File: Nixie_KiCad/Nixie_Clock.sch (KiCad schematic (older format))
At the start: 34 parts, among them U1 K155ID1, U10 K155ID1, U11 IN-14, U12 K155ID1, U13 IN-14, U14 DS3231, U2 IN-14, U3 K155ID1, U4 IN-14, U5 K155ID1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

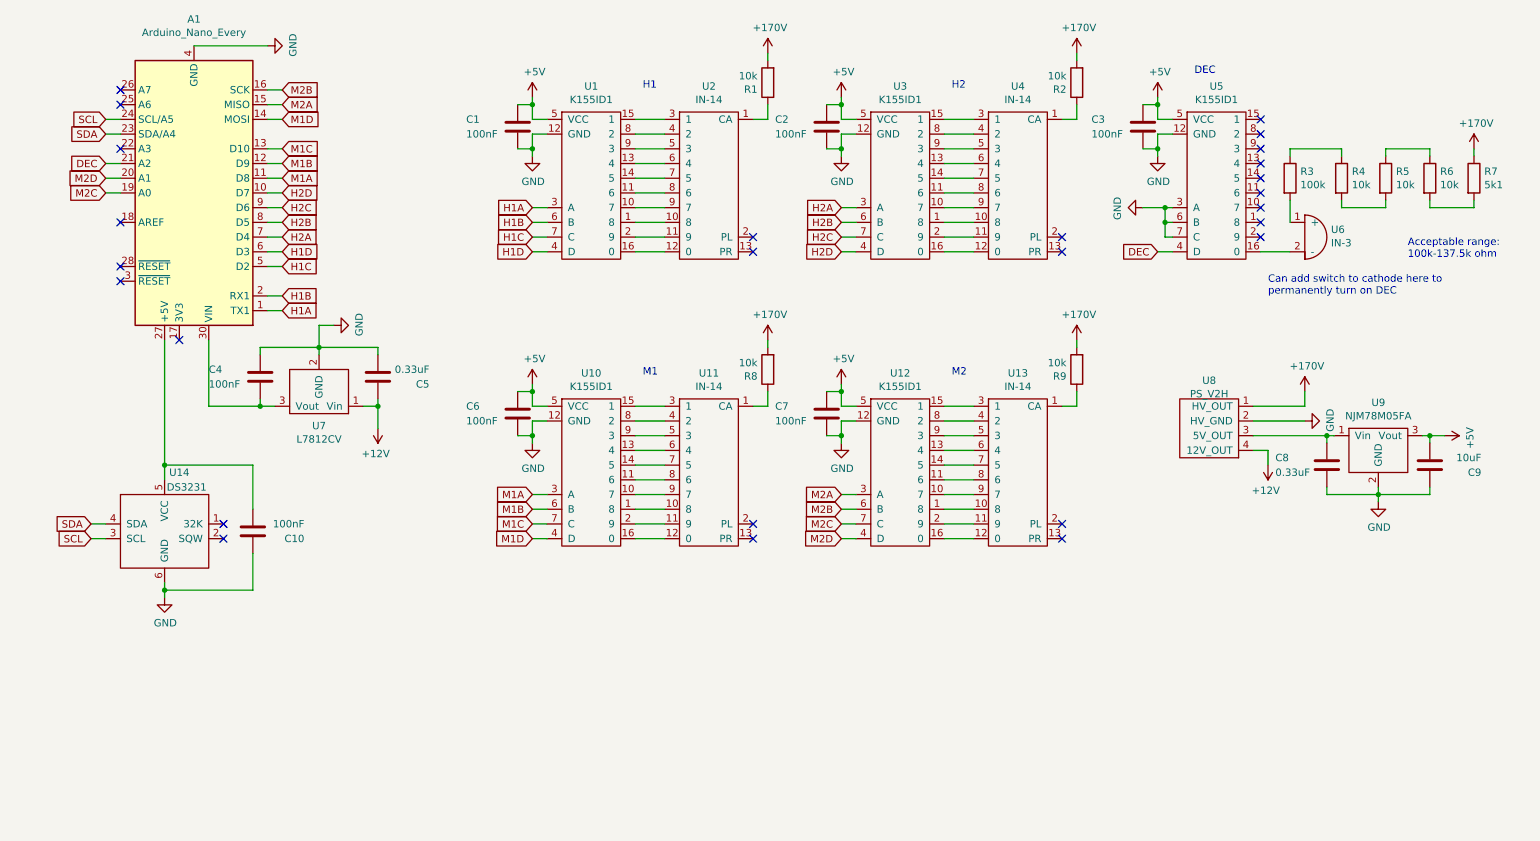
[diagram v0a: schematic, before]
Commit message: updated schematic to 2.0
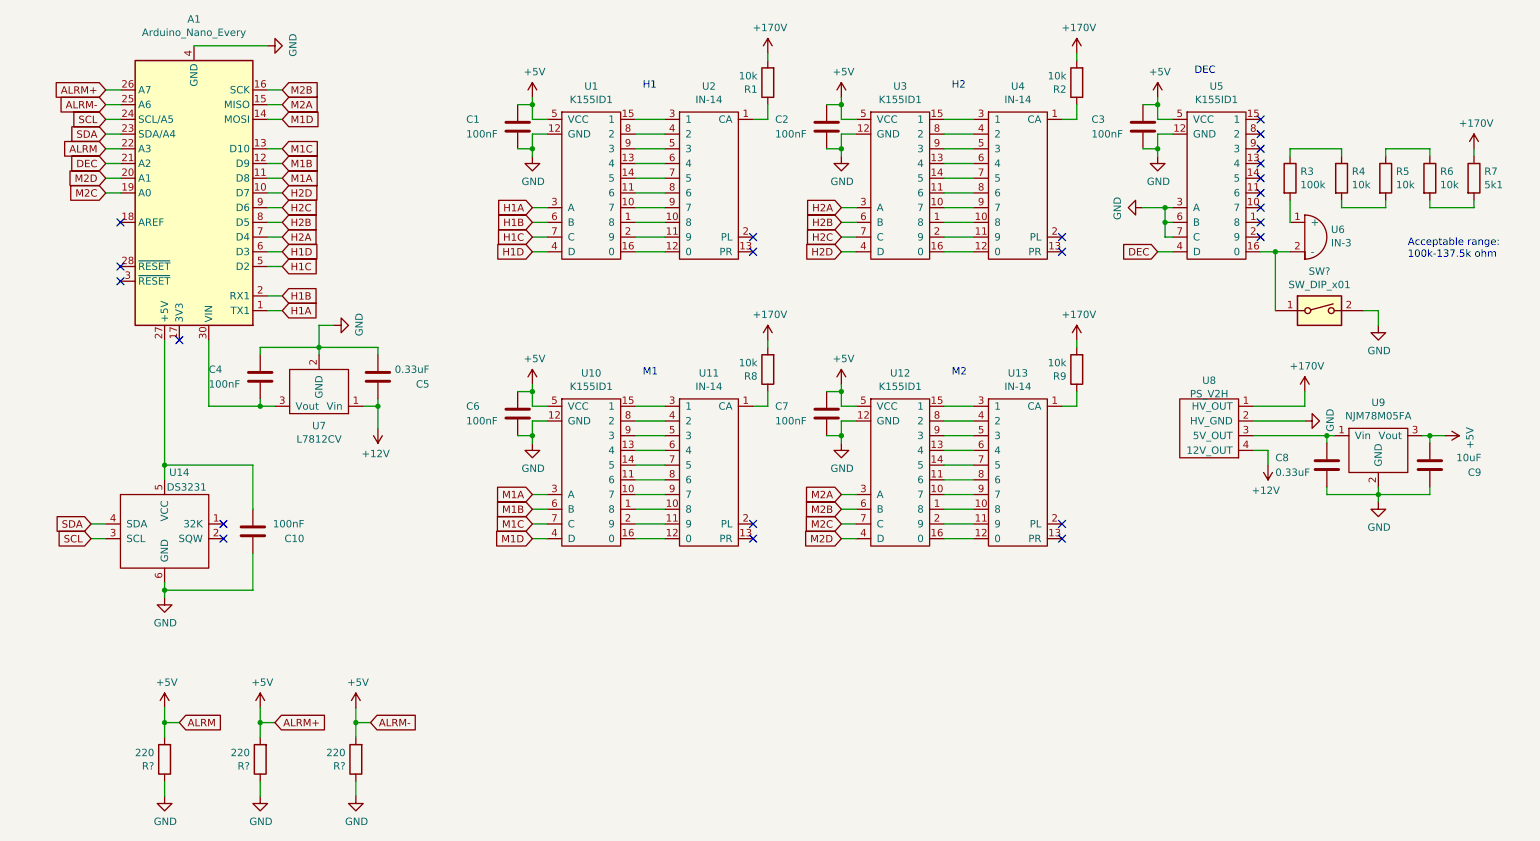
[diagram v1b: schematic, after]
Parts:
- added R? (x3): 220, Resistor_THT:R_Axial_DIN0207_L6.3mm_D2.5mm_P7.62mm_Horizontal, symbol Device:R
- added SW?: SW_DIP_x01, symbol Switch:SW_DIP_x01
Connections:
- net +5V: now also A1.22 (A3), A1.25 (A6), A1.26 (A7), R?.2, R?.2, R?.2
- net GND: now also R?.1, R?.1, R?.1, SW?.2
- net at U5.16 (0), U6.2 (-): now also SW?.1
- no-connect marks 26 -> 23
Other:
- note removed: "Can add switch to cathode here to\npermanently turn on DEC"
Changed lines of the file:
@@
 Title "Nixie Clock"
 Date "2022-01-07"
-Rev "1.1.1"
+Rev "2.0"
 Comp "Michael Zheng"
 Comment1 ""
@@
 $EndComp
 Wire Wire Line
-	9150 3450 8950 3450
+	9150 3450 9050 3450
 $Comp
 L Nixie_Lib:+170V #PWR017
@@
 Wire Wire Line
 	10400 2750 10400 2800
-Text Notes 9000 3750 0    50   ~ 0
-Can add switch to cathode here to\npermanently turn on DEC
 Wire Wire Line
 	2300 2450 2200 2450
 Wire Wire Line
 	2200 2350 2300 2350
-NoConn ~ 1200 2350
-NoConn ~ 1200 2450
-NoConn ~ 1200 2750
 NoConn ~ 1200 3250
 NoConn ~ 1200 3550
 NoConn ~ 1200 3650
 NoConn ~ 1600 4050
-$Comp
-L Nixie_Lib:Arduino_Nano_Every A1
-U 1 1 61EA91F0
-P 1700 3050
-F 0 "A1" H 1700 1869 50  0000 C CNN
-F 1 "Arduino_Nano_Every" H 1700 1960 50  0000 C CNN
-F 2 "Module:Arduino_Nano" H 1700 3050 50  0001 C CIN
-F 3 "https://content.arduino.cc/assets/NANOEveryV3.0_sch.pdf" H 1700 3050 50  0001 C CNN
-	1    1700 3050
-	-1   0    0    1
-$EndComp
 $Comp
 L power:GND #PWR024
@@
 Wire Wire Line
 	1100 2550 1200 2550
+$Comp
+L Switch:SW_DIP_x01 SW?
+U 1 1 61DB88E1
+P 9350 3850
+F 0 "SW?" H 9350 4117 50  0000 C CNN
+F 1 "SW_DIP_x01" H 9350 4026 50  0000 C CNN
+F 2 "" H 9350 3850 50  0001 C CNN
+F 3 "~" H 9350 3850 50  0001 C CNN
+	1    9350 3850
+	1    0    0    -1
+$EndComp
+Connection ~ 9050 3450
+Wire Wire Line
+	9050 3450 8950 3450
+$Comp
+L power:GND #PWR?
+U 1 1 61DC508D
+P 9750 3950
+F 0 "#PWR?" H 9750 3700 50  0001 C CNN
+F 1 "GND" H 9755 3777 50  0000 C CNN
+F 2 "" H 9750 3950 50  0001 C CNN
+F 3 "" H 9750 3950 50  0001 C CNN
+	1    9750 3950
+	1    0    0    -1
+$EndComp
+Wire Wire Line
+	9050 3450 9050 3850
+Wire Wire Line
+	9650 3850 9750 3850
+Wire Wire Line
+	9750 3850 9750 3950
+Text GLabel 1100 2750 0    50   Input ~ 0
+ALRM
+Text GLabel 1100 2350 0    50   Input ~ 0
+ALRM+
+Text GLabel 1100 2450 0    50   Input ~ 0
+ALRM-
+Wire Wire Line
+	1100 2350 1200 2350
+$Comp
+L Nixie_Lib:Arduino_Nano_Every A1
+U 1 1 61EA91F0
+P 1700 3050
+F 0 "A1" H 1700 1869 50  0000 C CNN
+F 1 "Arduino_Nano_Every" H 1700 1960 50  0000 C CNN
+F 2 "Module:Arduino_Nano" H 1700 3050 50  0001 C CIN
+F 3 "https://content.arduino.cc/assets/NANOEveryV3.0_sch.pdf" H 1700 3050 50  0001 C CNN
+	1    1700 3050
+	-1   0    0    1
+$EndComp
+Wire Wire Line
+	1100 2450 1200 2450
+Wire Wire Line
+	1100 2750 1200 2750
+$Comp
+L Device:R R?
+U 1 1 61E7D12A
+P 1500 6900
+F 0 "R?" H 1570 6946 50  0000 L CNN
+F 1 "220" H 1570 6855 50  0000 L CNN
+F 2 "Resistor_THT:R_Axial_DIN0207_L6.3mm_D2.5mm_P7.62mm_Horizontal" V 1430 6900 50  0001 C CNN
+F 3 "~" H 1500 6900 50  0001 C CNN
+	1    1500 6900
+	-1   0    0    1
+$EndComp
+$Comp
+L power:GND #PWR?
+U 1 1 61E7D6BF
+P 1500 7150
+F 0 "#PWR?" H 1500 6900 50  0001 C CNN
+F 1 "GND" H 1505 6977 50  0000 C CNN
+F 2 "" H 1500 7150 50  0001 C CNN
+F 3 "" H 1500 7150 50  0001 C CNN
+	1    1500 7150
+	1    0    0    -1
+$EndComp
+$Comp
+L power:+5V #PWR?
+U 1 1 61E8ADEA
+P 1500 6550
+F 0 "#PWR?" H 1500 6400 50  0001 C CNN
+F 1 "+5V" H 1515 6723 50  0000 C CNN
+F 2 "" H 1500 6550 50  0001 C CNN
+F 3 "" H 1500 6550 50  0001 C CNN
+	1    1500 6550
+	1    0    0    -1
+$EndComp
+Wire Wire Line
+	1500 7150 1500 7050
+Wire Wire Line
+	1500 6550 1500 6650
+Text GLabel 1600 6650 2    50   Input ~ 0
+ALRM
+Wire Wire Line
+	1500 6650 1600 6650
+Connection ~ 1500 6650
+Wire Wire Line
+	1500 6650 1500 6750
+$Comp
+L Device:R R?
+U 1 1 61EC38AF
+P 2150 6900
+F 0 "R?" H 2220 6946 50  0000 L CNN
+F 1 "220" H 2220 6855 50  0000 L CNN
+F 2 "Resistor_THT:R_Axial_DIN0207_L6.3mm_D2.5mm_P7.62mm_Horizontal" V 2080 6900 50  0001 C CNN
+F 3 "~" H 2150 6900 50  0001 C CNN
+	1    2150 6900
+	-1   0    0    1
+$EndComp
+$Comp
+L power:+5V #PWR?
+U 1 1 61EC3F05
+P 2150 6550
+F 0 "#PWR?" H 2150 6400 50  0001 C CNN
+F 1 "+5V" H 2165 6723 50  0000 C CNN
+F 2 "" H 2150 6550 50  0001 C CNN
+F 3 "" H 2150 6550 50  0001 C CNN
+	1    2150 6550
+	1    0    0    -1
+$EndComp
+$Comp
+L power:GND #PWR?
+U 1 1 61EC4290
+P 2150 7150
+F 0 "#PWR?" H 2150 6900 50  0001 C CNN
+F 1 "GND" H 2155 6977 50  0000 C CNN
+F 2 "" H 2150 7150 50  0001 C CNN
+F 3 "" H 2150 7150 50  0001 C CNN
+	1    2150 7150
+	1    0    0    -1
+$EndComp
+Wire Wire Line
+	2150 6550 2150 6650
+Wire Wire Line
+	2150 7050 2150 7150
+Wire Wire Line
+	2150 6650 2250 6650
+Connection ~ 2150 6650
+Wire Wire Line
+	2150 6650 2150 6750
+Text GLabel 2250 6650 2    50   Input ~ 0
+ALRM+
+$Comp
+L Device:R R?
+U 1 1 61EFBDFE
+P 2800 6900
+F 0 "R?" H 2870 6946 50  0000 L CNN
+F 1 "220" H 2870 6855 50  0000 L CNN
+F 2 "Resistor_THT:R_Axial_DIN0207_L6.3mm_D2.5mm_P7.62mm_Horizontal" V 2730 6900 50  0001 C CNN
+F 3 "~" H 2800 6900 50  0001 C CNN
+	1    2800 6900
+	-1   0    0    1
+$EndComp
+$Comp
+L power:+5V #PWR?
+U 1 1 61EFCF7D
+P 2800 6550
+F 0 "#PWR?" H 2800 6400 50  0001 C CNN
+F 1 "+5V" H 2815 6723 50  0000 C CNN
+F 2 "" H 2800 6550 50  0001 C CNN
+F 3 "" H 2800 6550 50  0001 C CNN
+	1    2800 6550
+	1    0    0    -1
+$EndComp
+$Comp
+L power:GND #PWR?
+U 1 1 61EFD250
+P 2800 7150
+F 0 "#PWR?" H 2800 6900 50  0001 C CNN
+F 1 "GND" H 2805 6977 50  0000 C CNN
+F 2 "" H 2800 7150 50  0001 C CNN
+F 3 "" H 2800 7150 50  0001 C CNN
+	1    2800 7150
+	1    0    0    -1
+$EndComp
+Wire Wire Line
+	2800 7050 2800 7150
+Wire Wire Line
+	2800 6750 2800 6650
+Wire Wire Line
+	2800 6650 2900 6650
+Connection ~ 2800 6650
+Wire Wire Line
+	2800 6650 2800 6550
+Text GLabel 2900 6650 2    50   Input ~ 0
+ALRM-
 $EndSCHEMATC

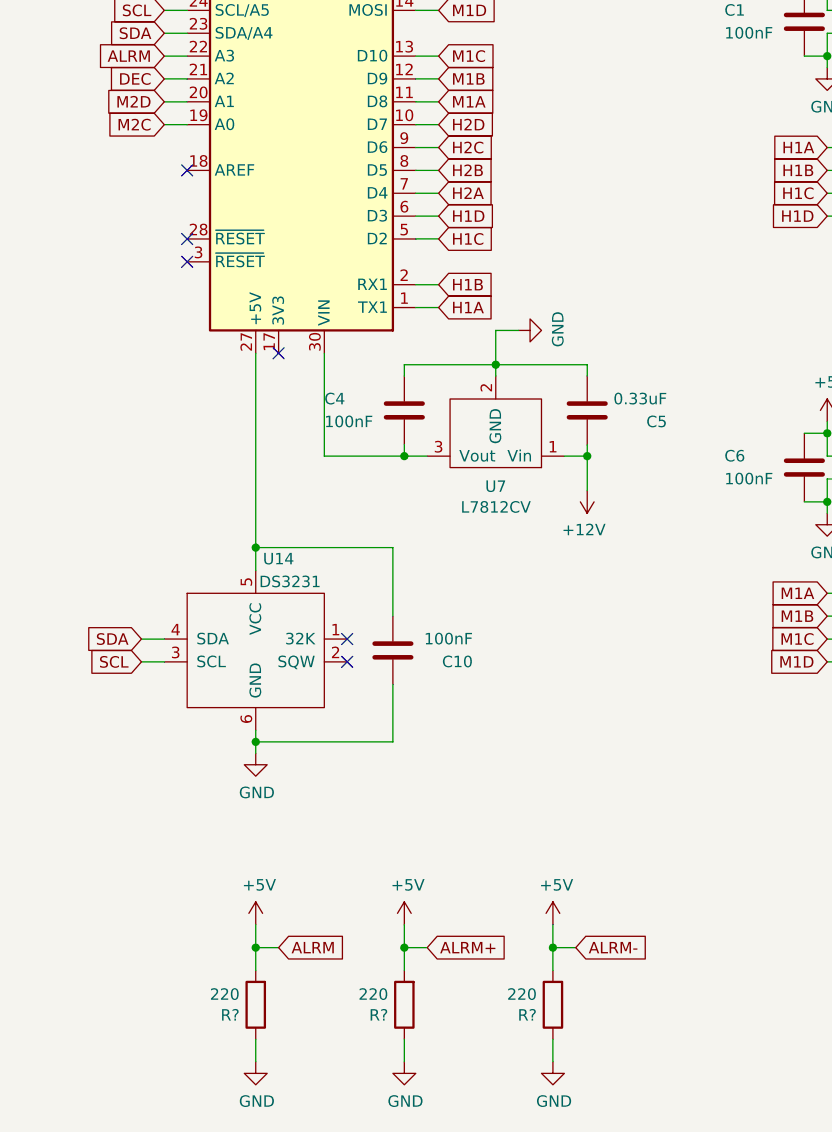
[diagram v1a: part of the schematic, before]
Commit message: updated to internal pull up resistors
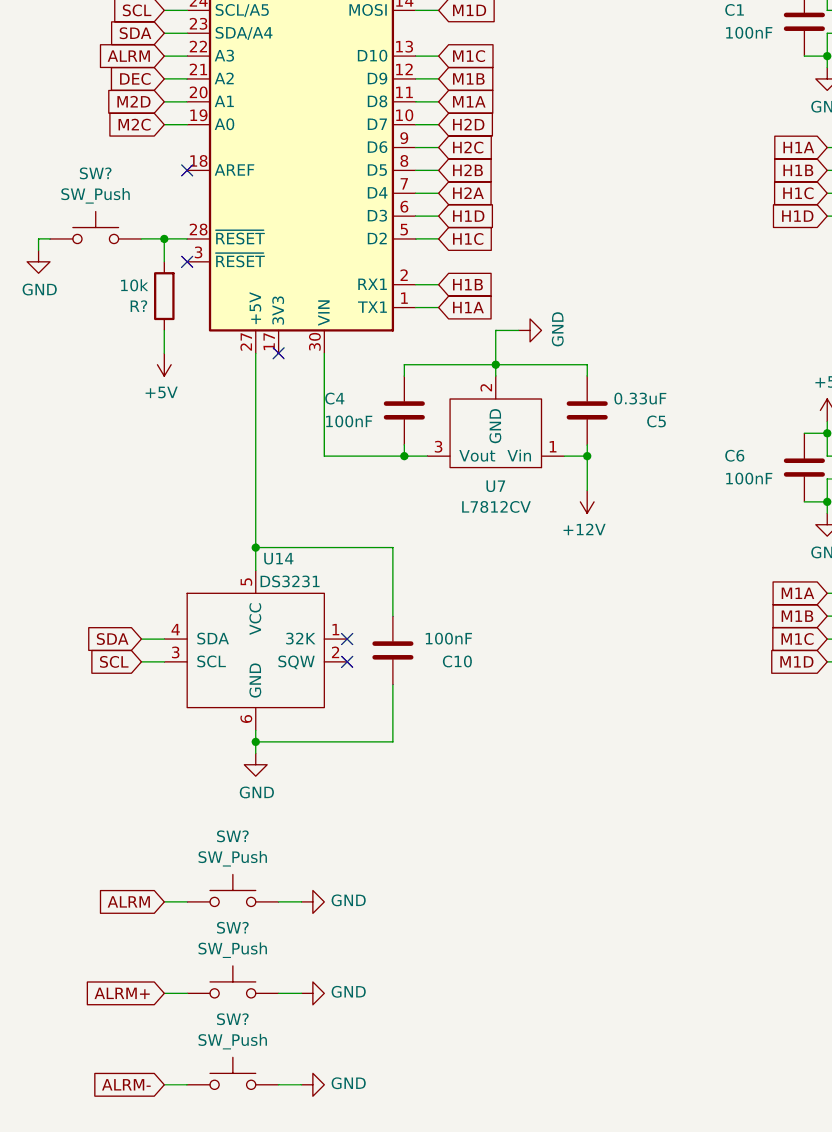
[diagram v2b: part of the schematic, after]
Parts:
- removed R? (x3): 220, Resistor_THT:R_Axial_DIN0207_L6.3mm_D2.5mm_P7.62mm_Horizontal, symbol Device:R
- added R?: 10k, Resistor_THT:R_Axial_DIN0207_L6.3mm_D2.5mm_P7.62mm_Horizontal, symbol Device:R
- added SW? (x4): SW_Push, symbol Switch:SW_Push
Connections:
- net +5V: now also R?.1; no longer A1.22 (A3), A1.25 (A6), A1.26 (A7)
- net GND: now also SW?.1, SW?.2, SW?.2, SW?.2
- net at A1.28 (~RESET): now also R?.2, SW?.2
- new net ALRM: A1.22 (A3), SW?.1
- new net ALRM+: A1.26 (A7), SW?.1
- new net ALRM-: A1.25 (A6), SW?.1
- no-connect marks 23 -> 22
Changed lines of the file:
@@
 	2200 2350 2300 2350
 NoConn ~ 1200 3250
-NoConn ~ 1200 3550
 NoConn ~ 1200 3650
 NoConn ~ 1600 4050
@@
 Wire Wire Line
 	1100 2750 1200 2750
+Text GLabel 1100 6450 0    50   Input ~ 0
+ALRM
+Text GLabel 1100 6850 0    50   Input ~ 0
+ALRM+
+Text GLabel 1100 7250 0    50   Input ~ 0
+ALRM-
+$Comp
+L Switch:SW_Push SW?
+U 1 1 61E3B7EB
+P 1400 6450
+F 0 "SW?" H 1400 6735 50  0000 C CNN
+F 1 "SW_Push" H 1400 6644 50  0000 C CNN
+F 2 "" H 1400 6650 50  0001 C CNN
+F 3 "~" H 1400 6650 50  0001 C CNN
+	1    1400 6450
+	1    0    0    -1
+$EndComp
+$Comp
+L power:GND #PWR?
+U 1 1 61E64086
+P 1700 6450
+F 0 "#PWR?" H 1700 6200 50  0001 C CNN
+F 1 "GND" V 1705 6322 50  0000 R CNN
+F 2 "" H 1700 6450 50  0001 C CNN
+F 3 "" H 1700 6450 50  0001 C CNN
+	1    1700 6450
+	0    -1   -1   0
+$EndComp
+$Comp
+L Switch:SW_Push SW?
+U 1 1 61E66E38
+P 1400 6850
+F 0 "SW?" H 1400 7135 50  0000 C CNN
+F 1 "SW_Push" H 1400 7044 50  0000 C CNN
+F 2 "" H 1400 7050 50  0001 C CNN
+F 3 "~" H 1400 7050 50  0001 C CNN
+	1    1400 6850
+	1    0    0    -1
+$EndComp
+$Comp
+L Switch:SW_Push SW?
+U 1 1 61E67592
+P 1400 7250
+F 0 "SW?" H 1400 7535 50  0000 C CNN
+F 1 "SW_Push" H 1400 7444 50  0000 C CNN
+F 2 "" H 1400 7450 50  0001 C CNN
+F 3 "~" H 1400 7450 50  0001 C CNN
+	1    1400 7250
+	1    0    0    -1
+$EndComp
+Wire Wire Line
+	1100 7250 1200 7250
+Wire Wire Line
+	1100 6850 1200 6850
+Wire Wire Line
+	1100 6450 1200 6450
+Wire Wire Line
+	1600 6450 1700 6450
+$Comp
+L power:GND #PWR?
+U 1 1 61E9C82E
+P 1700 6850
+F 0 "#PWR?" H 1700 6600 50  0001 C CNN
+F 1 "GND" V 1705 6722 50  0000 R CNN
+F 2 "" H 1700 6850 50  0001 C CNN
+F 3 "" H 1700 6850 50  0001 C CNN
+	1    1700 6850
+	0    -1   -1   0
+$EndComp
+$Comp
+L power:GND #PWR?
+U 1 1 61E9CC91
+P 1700 7250
+F 0 "#PWR?" H 1700 7000 50  0001 C CNN
+F 1 "GND" V 1705 7122 50  0000 R CNN
+F 2 "" H 1700 7250 50  0001 C CNN
+F 3 "" H 1700 7250 50  0001 C CNN
+	1    1700 7250
+	0    -1   -1   0
+$EndComp
+Wire Wire Line
+	1600 6850 1700 6850
+Wire Wire Line
+	1600 7250 1700 7250
+$Comp
+L Switch:SW_Push SW?
+U 1 1 61EC755B
+P 800 3550
+F 0 "SW?" H 800 3835 50  0000 C CNN
+F 1 "SW_Push" H 800 3744 50  0000 C CNN
+F 2 "" H 800 3750 50  0001 C CNN
+F 3 "~" H 800 3750 50  0001 C CNN
+	1    800  3550
+	1    0    0    -1
+$EndComp
+$Comp
+L power:GND #PWR?
+U 1 1 61EC8AAB
+P 550 3600
+F 0 "#PWR?" H 550 3350 50  0001 C CNN
+F 1 "GND" H 555 3427 50  0000 C CNN
+F 2 "" H 550 3600 50  0001 C CNN
+F 3 "" H 550 3600 50  0001 C CNN
+	1    550  3600
+	1    0    0    -1
+$EndComp
+Wire Wire Line
+	600  3550 550  3550
+Wire Wire Line
+	550  3550 550  3600
 $Comp
 L Device:R R?
-U 1 1 61E7D12A
-P 1500 6900
-F 0 "R?" H 1570 6946 50  0000 L CNN
-F 1 "220" H 1570 6855 50  0000 L CNN
-F 2 "Resistor_THT:R_Axial_DIN0207_L6.3mm_D2.5mm_P7.62mm_Horizontal" V 1430 6900 50  0001 C CNN
-F 3 "~" H 1500 6900 50  0001 C CNN
-	1    1500 6900
-	-1   0    0    1
-$EndComp
-$Comp
-L power:GND #PWR?
-U 1 1 61E7D6BF
-P 1500 7150
-F 0 "#PWR?" H 1500 6900 50  0001 C CNN
-F 1 "GND" H 1505 6977 50  0000 C CNN
-F 2 "" H 1500 7150 50  0001 C CNN
-F 3 "" H 1500 7150 50  0001 C CNN
-	1    1500 7150
-	1    0    0    -1
-$EndComp
+U 1 1 61ED925B
+P 1100 3800
+F 0 "R?" H 1170 3846 50  0000 L CNN
+F 1 "10k" H 1170 3755 50  0000 L CNN
+F 2 "Resistor_THT:R_Axial_DIN0207_L6.3mm_D2.5mm_P7.62mm_Horizontal" V 1030 3800 50  0001 C CNN
+F 3 "~" H 1100 3800 50  0001 C CNN
+	1    1100 3800
+	-1   0    0    1
+$EndComp
+Wire Wire Line
+	1000 3550 1100 3550
+Wire Wire Line
+	1100 3650 1100 3550
+Connection ~ 1100 3550
+Wire Wire Line
+	1100 3550 1200 3550
 $Comp
 L power:+5V #PWR?
-U 1 1 61E8ADEA
-P 1500 6550
-F 0 "#PWR?" H 1500 6400 50  0001 C CNN
-F 1 "+5V" H 1515 6723 50  0000 C CNN
-F 2 "" H 1500 6550 50  0001 C CNN
-F 3 "" H 1500 6550 50  0001 C CNN
-	1    1500 6550
-	1    0    0    -1
-$EndComp
-Wire Wire Line
-	1500 7150 1500 7050
-Wire Wire Line
-	1500 6550 1500 6650
-Text GLabel 1600 6650 2    50   Input ~ 0
-ALRM
-Wire Wire Line
-	1500 6650 1600 6650
-Connection ~ 1500 6650
-Wire Wire Line
-	1500 6650 1500 6750
-$Comp
-L Device:R R?
-U 1 1 61EC38AF
-P 2150 6900
-F 0 "R?" H 2220 6946 50  0000 L CNN
-F 1 "220" H 2220 6855 50  0000 L CNN
-F 2 "Resistor_THT:R_Axial_DIN0207_L6.3mm_D2.5mm_P7.62mm_Horizontal" V 2080 6900 50  0001 C CNN
-F 3 "~" H 2150 6900 50  0001 C CNN
-	1    2150 6900
-	-1   0    0    1
-$EndComp
-$Comp
-L power:+5V #PWR?
-U 1 1 61EC3F05
-P 2150 6550
-F 0 "#PWR?" H 2150 6400 50  0001 C CNN
-F 1 "+5V" H 2165 6723 50  0000 C CNN
-F 2 "" H 2150 6550 50  0001 C CNN
-F 3 "" H 2150 6550 50  0001 C CNN
-	1    2150 6550
-	1    0    0    -1
-$EndComp
-$Comp
-L power:GND #PWR?
-U 1 1 61EC4290
-P 2150 7150
-F 0 "#PWR?" H 2150 6900 50  0001 C CNN
-F 1 "GND" H 2155 6977 50  0000 C CNN
-F 2 "" H 2150 7150 50  0001 C CNN
-F 3 "" H 2150 7150 50  0001 C CNN
-	1    2150 7150
-	1    0    0    -1
-$EndComp
-Wire Wire Line
-	2150 6550 2150 6650
-Wire Wire Line
-	2150 7050 2150 7150
-Wire Wire Line
-	2150 6650 2250 6650
-Connection ~ 2150 6650
-Wire Wire Line
-	2150 6650 2150 6750
-Text GLabel 2250 6650 2    50   Input ~ 0
-ALRM+
-$Comp
-L Device:R R?
-U 1 1 61EFBDFE
-P 2800 6900
-F 0 "R?" H 2870 6946 50  0000 L CNN
-F 1 "220" H 2870 6855 50  0000 L CNN
-F 2 "Resistor_THT:R_Axial_DIN0207_L6.3mm_D2.5mm_P7.62mm_Horizontal" V 2730 6900 50  0001 C CNN
-F 3 "~" H 2800 6900 50  0001 C CNN
-	1    2800 6900
-	-1   0    0    1
-$EndComp
-$Comp
-L power:+5V #PWR?
-U 1 1 61EFCF7D
-P 2800 6550
-F 0 "#PWR?" H 2800 6400 50  0001 C CNN
-F 1 "+5V" H 2815 6723 50  0000 C CNN
-F 2 "" H 2800 6550 50  0001 C CNN
-F 3 "" H 2800 6550 50  0001 C CNN
-	1    2800 6550
-	1    0    0    -1
-$EndComp
-$Comp
-L power:GND #PWR?
-U 1 1 61EFD250
-P 2800 7150
-F 0 "#PWR?" H 2800 6900 50  0001 C CNN
-F 1 "GND" H 2805 6977 50  0000 C CNN
-F 2 "" H 2800 7150 50  0001 C CNN
-F 3 "" H 2800 7150 50  0001 C CNN
-	1    2800 7150
-	1    0    0    -1
-$EndComp
-Wire Wire Line
-	2800 7050 2800 7150
-Wire Wire Line
-	2800 6750 2800 6650
-Wire Wire Line
-	2800 6650 2900 6650
-Connection ~ 2800 6650
-Wire Wire Line
-	2800 6650 2800 6550
-Text GLabel 2900 6650 2    50   Input ~ 0
-ALRM-
+U 1 1 61EF7D8B
+P 1100 4050
+F 0 "#PWR?" H 1100 3900 50  0001 C CNN
+F 1 "+5V" H 1115 4223 50  0000 C CNN
+F 2 "" H 1100 4050 50  0001 C CNN
+F 3 "" H 1100 4050 50  0001 C CNN
+	1    1100 4050
+	-1   0    0    1
+$EndComp
+Wire Wire Line
+	1100 3950 1100 4050
 $EndSCHEMATC
